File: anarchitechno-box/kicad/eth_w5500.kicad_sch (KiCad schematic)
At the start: 35 parts, among them U16 W5500, U17 ARJM11B1-009-AB-EW2, Y1 25MHz

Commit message: Stijn in de Trein
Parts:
- D8, D9: footprint LED_SMD:LED_0805_2012Metric -> LED_SMD:LED_0603_1608Metric
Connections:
- net +3.3V: no longer C54.1, FB1.1
- net +3V3: now also C54.1, FB1.1
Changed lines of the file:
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@@
 			)
 		)
-		(property "Footprint" "LED_SMD:LED_0805_2012Metric"
+		(property "Footprint" "LED_SMD:LED_0603_1608Metric"
 			(at 152.4 107.95 0)
 			(effects
@@
 	)
 	(symbol
+		(lib_id "power:+3V3")
+		(at 88.9 24.13 0)
+		(unit 1)
+		(exclude_from_sim no)
+		(in_bom yes)
+		(on_board yes)
+		(dnp no)
+		(fields_autoplaced yes)
+		(property "Reference" "#PWR0155"
+			(at 88.9 27.94 0)
+			(effects
+				(font
+					(size 1.27 1.27)
+				)
+				(hide yes)
+			)
+		)
+		(property "Value" "+3V3"
+			(at 88.9 19.05 0)
+			(effects
+				(font
+					(size 1.27 1.27)
+				)
+			)
+		)
+		(property "Footprint" ""
+			(at 88.9 24.13 0)
+			(effects
+				(font
+					(size 1.27 1.27)
+				)
+				(hide yes)
+			)
+		)
+		(property "Datasheet" ""
+			(at 88.9 24.13 0)
+			(effects
+				(font
+					(size 1.27 1.27)
+				)
+				(hide yes)
+			)
+		)
+		(property "Description" "Power symbol creates a global label with name \"+3V3\""
+			(at 88.9 24.13 0)
+			(effects
+				(font
+					(size 1.27 1.27)
+				)
+				(hide yes)
+			)
+		)
+		(pin "1"
+		)
+		(instances
+			(project "anarchytechnobox"
+				(path "/8c734c41-38ed-40fc-83bd-134786dcfb35/fe979741-96bb-4de4-ad6e-25369264489a"
+					(reference "#PWR0155")
+					(unit 1)
+				)
+			)
+		)
+	)
+	(symbol
 		(lib_id "power:GND")
 		(at 46.99 116.84 0)
@@
 			)
 		)
-		(property "Footprint" "LED_SMD:LED_0805_2012Metric"
+		(property "Footprint" "LED_SMD:LED_0603_1608Metric"
 			(at 152.4 113.03 0)
 			(effects
@@
 					(unit 1)
 				)
-			)
-		)
-	)
-	(symbol
-		(lib_id "power:+3.3V")
-		(at 88.9 24.13 0)
-		(unit 1)
-		(exclude_from_sim no)
-		(in_bom yes)
-		(on_board yes)
-		(dnp no)
-		(fields_autoplaced yes)
-		(property "Reference" "#PWR0117"
-			(at 88.9 27.94 0)
-			(effects
-				(font
-					(size 1.27 1.27)
-				)
-				(hide yes)
-			)
-		)
-		(property "Value" "+3.3V"
-			(at 88.9 19.05 0)
-			(effects
-				(font
-					(size 1.27 1.27)
-				)
-			)
-		)
-		(property "Footprint" ""
-			(at 88.9 24.13 0)
-			(effects
-				(font
-					(size 1.27 1.27)
-				)
-				(hide yes)
-			)
-		)
-		(property "Datasheet" ""
-			(at 88.9 24.13 0)
-			(effects
-				(font
-					(size 1.27 1.27)
-				)
-				(hide yes)
-			)
-		)
-		(property "Description" "Power symbol creates a global label with name \"+3.3V\""
-			(at 88.9 24.13 0)
-			(effects
-				(font
-					(size 1.27 1.27)
-				)
-				(hide yes)
-			)
-		)
-		(pin "1"
-		)
-		(instances
-			(project "anarchytechnobox"
-				(path "/8c734c41-38ed-40fc-83bd-134786dcfb35/fe979741-96bb-4de4-ad6e-25369264489a"
-					(reference "#PWR0117")
-					(unit 1)
-				)

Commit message: meer Stijn in de Trein
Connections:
- net +3.3V is gone; now on net +3V3: R30.1, R31.1, R32.1, R33.1, R34.1
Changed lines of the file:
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@@
+	)
+	(symbol
+		(lib_id "power:+3V3")
+		(at 199.39 57.15 0)
+		(unit 1)
+		(exclude_from_sim no)
+		(in_bom yes)
+		(on_board yes)
+		(dnp no)
+		(fields_autoplaced yes)
+		(property "Reference" "#PWR0117"
+			(at 199.39 60.96 0)
+			(effects
+				(font
+					(size 1.27 1.27)
+				)
+				(hide yes)
+			)
+		)
+		(property "Value" "+3V3"
+			(at 199.39 52.07 0)
+			(effects
+				(font
+					(size 1.27 1.27)
+				)
+			)
+		)
+		(property "Footprint" ""
+			(at 199.39 57.15 0)
+			(effects
+				(font
+					(size 1.27 1.27)
+				)
+				(hide yes)
+			)
+		)
+		(property "Datasheet" ""
+			(at 199.39 57.15 0)
+			(effects
+				(font
+					(size 1.27 1.27)
+				)
+				(hide yes)
+			)
+		)
+		(property "Description" "Power symbol creates a global label with name \"+3V3\""
+			(at 199.39 57.15 0)
+			(effects
+				(font
+					(size 1.27 1.27)
+				)
+				(hide yes)
+			)
+		)
+		(pin "1"
+		)
+		(instances
+			(project "anarchytechnobox"
+				(path "/8c734c41-38ed-40fc-83bd-134786dcfb35/fe979741-96bb-4de4-ad6e-25369264489a"
+					(reference "#PWR0117")
+					(unit 1)
+				)
+			)
+		)
 	)
 	(symbol
@@
 					(unit 1)
 				)
-			)
-		)
-	)
-	(symbol
-		(lib_id "power:+3.3V")
-		(at 199.39 57.15 0)
-		(unit 1)
-		(exclude_from_sim no)
-		(in_bom yes)
-		(on_board yes)
-		(dnp no)
-		(fields_autoplaced yes)
-		(property "Reference" "#PWR0129"
-			(at 199.39 60.96 0)
-			(effects
-				(font
-					(size 1.27 1.27)
-				)
-				(hide yes)
-			)
-		)
-		(property "Value" "+3.3V"
-			(at 199.39 52.07 0)
-			(effects
-				(font
-					(size 1.27 1.27)
-				)
-			)
-		)
-		(property "Footprint" ""
-			(at 199.39 57.15 0)
-			(effects
-				(font
-					(size 1.27 1.27)
-				)
-				(hide yes)
-			)
-		)
-		(property "Datasheet" ""
-			(at 199.39 57.15 0)
-			(effects
-				(font
-					(size 1.27 1.27)
-				)
-				(hide yes)
-			)
-		)
-		(property "Description" "Power symbol creates a global label with name \"+3.3V\""
-			(at 199.39 57.15 0)
-			(effects
-				(font
-					(size 1.27 1.27)
-				)
-				(hide yes)
-			)
-		)
-		(pin "1"
-		)
-		(instances
-			(project "anarchytechnobox"
-				(path "/8c734c41-38ed-40fc-83bd-134786dcfb35/fe979741-96bb-4de4-ad6e-25369264489a"
-					(reference "#PWR0129")
-					(unit 1)
-				)

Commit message: trein trein trein
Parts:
- removed C54: 100nF, Capacitor_SMD:C_0402_1005Metric, symbol Device:C
- removed FB1: BLM18PG121SN1D, Inductor_SMD:L_0603_1608Metric, symbol Device:FerriteBead
- added C54, C95: 100n, Capacitor_SMD:C_0402_1005Metric, symbol Device:C_Small
- added C94, C96: 10uF, Capacitor_SMD:C_0603_1608Metric, symbol Device:C
- added L2: BLM18PG121SN1D_C14709, BigFishImports:L0603, symbol BigFishImports:BLM18PG121SN1D_C14709
- added U1: LP5907MFX-3.3, Package_TO_SOT_SMD:SOT-23-5, symbol Regulator_Linear:LP5907MFX-3.3
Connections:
- net +3.3VA: now also C95.2, C96.1, U1.5 (OUT)
- net +3V3: now also U1.3 (EN)
- net GND: now also C54.1, C94.2, C95.1, C96.2, U1.2 (GND)
- new net +5V: L2.1
- new net 5V_ethernet_filtered: C54.2, C94.1, L2.2, U1.1 (IN)

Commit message: 100mbit ethernet jack
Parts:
- U17: footprint Footprints:ARJM11B1-009-AB-EW2 -> parts:ARJM11B1-009-AB-EW2
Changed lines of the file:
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@@
 			)
 		)
-		(property "Footprint" "Footprints:ARJM11B1-009-AB-EW2"
+		(property "Footprint" "parts:ARJM11B1-009-AB-EW2"
 			(at 212.09 74.93 0)
 			(effects

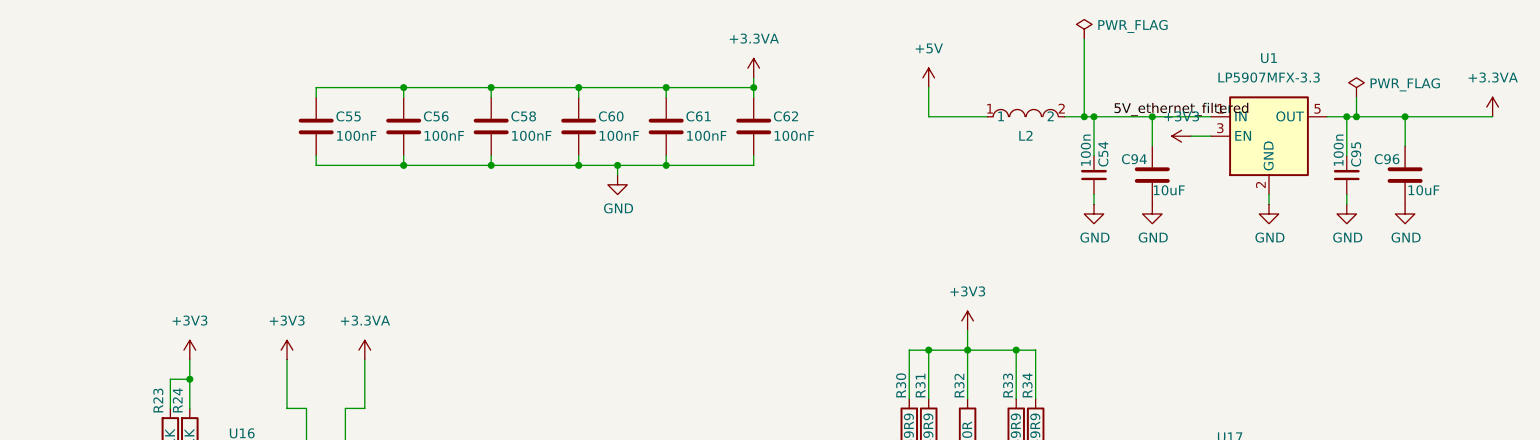
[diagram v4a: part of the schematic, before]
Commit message: Re-added 1.1V regulator. Removed 3.3VDDA for Ethernet. Increased clearances on layout a bit..
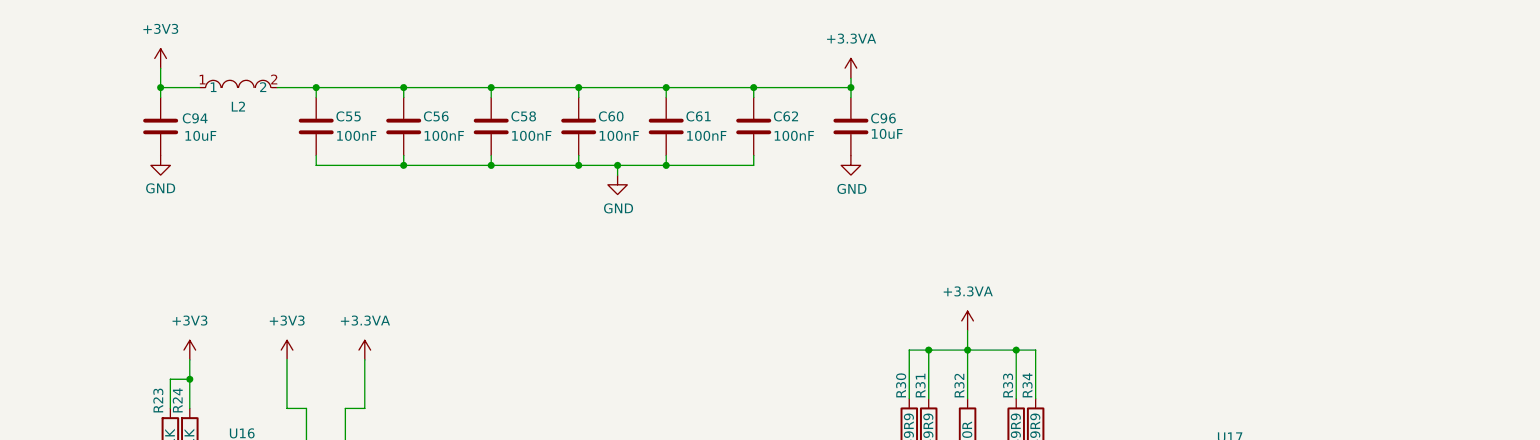
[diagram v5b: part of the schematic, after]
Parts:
- removed C54, C95: 100n, Capacitor_SMD:C_0402_1005Metric, symbol Device:C_Small
- removed U1: LP5907MFX-3.3, Package_TO_SOT_SMD:SOT-23-5, symbol Regulator_Linear:LP5907MFX-3.3
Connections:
- net +5V is gone; now on net +3V3: L2.1
- net +3.3VA: now also L2.2, R30.1, R31.1, R32.1, R33.1, R34.1
- net +3V3: now also C94.1; no longer R30.1, R31.1, R32.1, R33.1, R34.1
- removed net 5V_ethernet_filtered: C94.1, L2.2
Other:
- moved on the sheet: C94, C96, L2

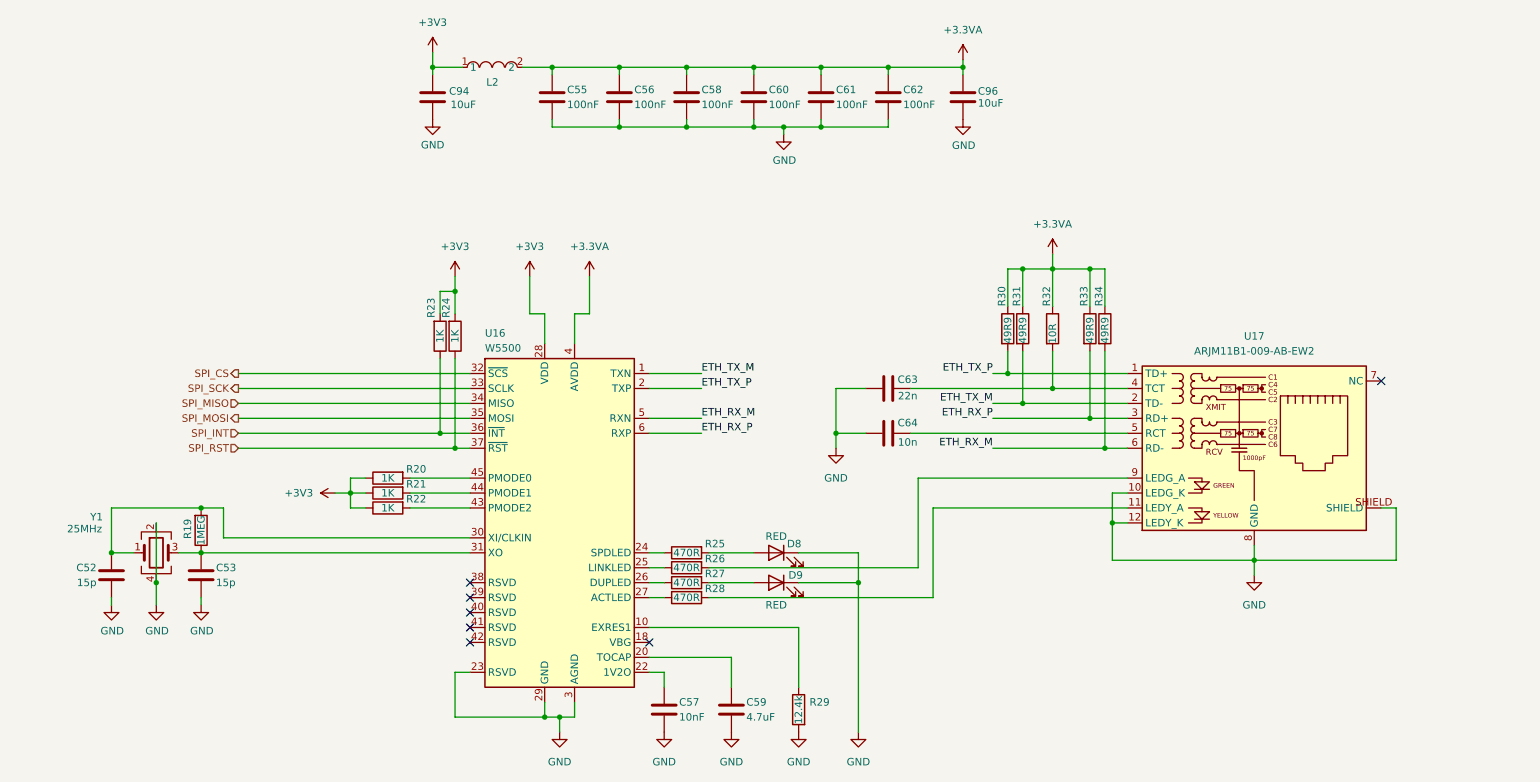
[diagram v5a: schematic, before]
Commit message: Schematic & PCB changes: - Cleaned up unnecessary electrolytic input capacitor flyback - Removed dual diode rectification on 5V, increased output capacitors - Feedback resistors DC/DCs set, enlarged for JLC basic parts - Sweep through schematic to consolidate caps to JLC basic parts (see list schematic front page) - Midi OUTPUT added (please check schematic) - Wiznet W5500 schematic reworked to RJ45 reference schematic: https://docs.wiznet.io/assets/files/w5500_sch_v110_use_mag_-dfff8bbb103d13be4f25cd2b2f8b950d.pdf - Replaced ethernet jack to HR911105A - Crystals chosen for W5500 and RP2350B (according to reference), 15pF load caps. - RS485 driver changed to SP3485EN for 3.3V operation - Replaced RS485 bus connectors with 2x RJ45s for passthrough - Groove connector replaced with JST XH 2mm - Added LCSC part numbers for various components in the schematic
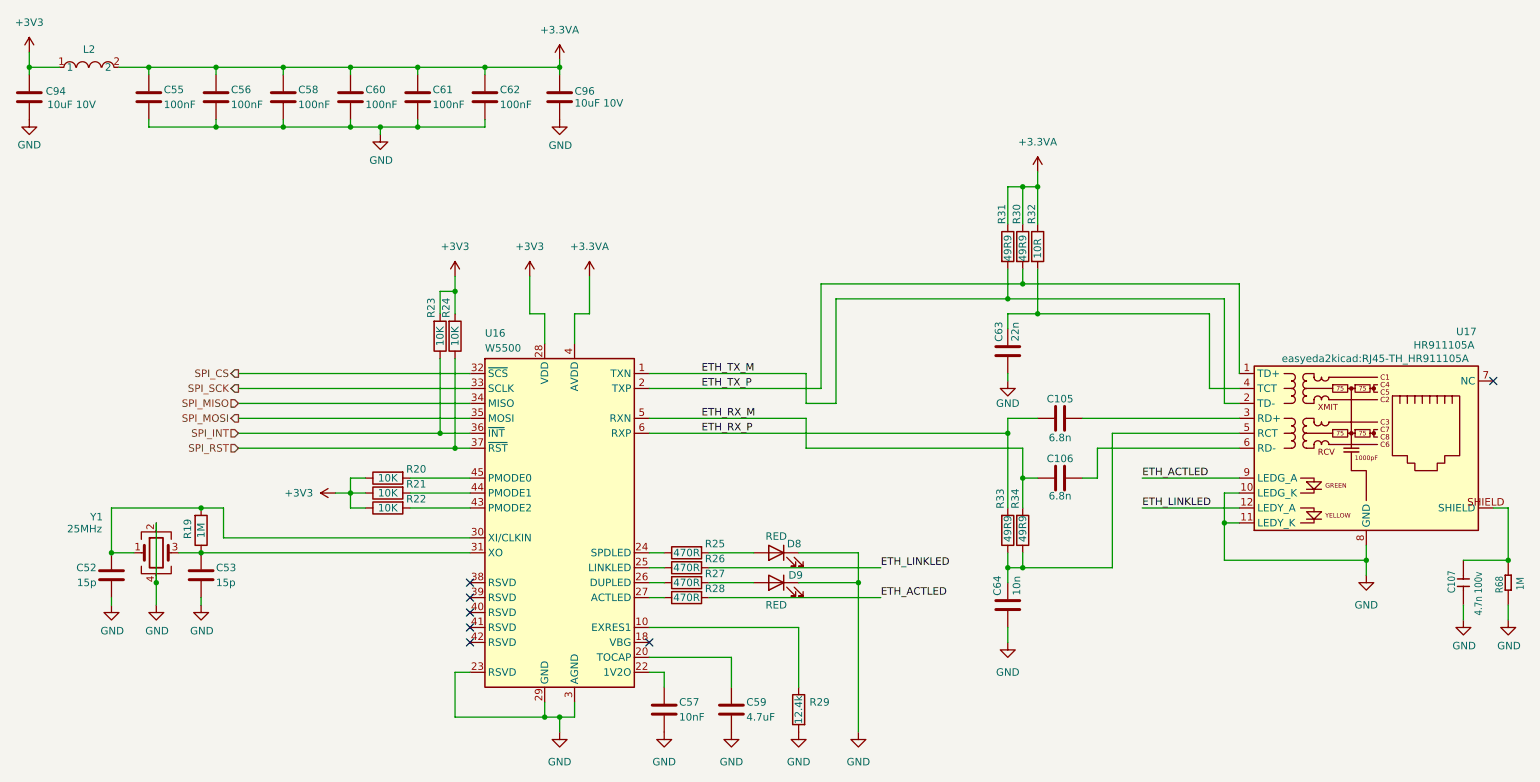
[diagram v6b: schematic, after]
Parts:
- added C105, C106: 6.8n, Capacitor_SMD:C_0603_1608Metric, symbol Device:C
- added C107: 4.7n 100v, Capacitor_SMD:C_1206_3216Metric, symbol TINRS - Wobbler (pico)sch-eagle-import:C-1206
- added R68: 1M, Resistor_SMD:R_0603_1608Metric, symbol TINRS - Wobbler (pico)sch-eagle-import:R-0603
- C52, C53: LCSC Part (none) -> C1548
- C57, C64: LCSC Part (none) -> C15195
- C59: LCSC Part (none) -> C19666
- C63: LCSC Part (none) -> C1532
- C94, C96: value 10uF -> 10uF 10V; Digi-Key_PN 311-1344-1-ND -> (none); LCSC Part (none) -> C19702
- L2: footprint BigFishImports:L0603 -> Inductor_SMD:L_0603_1608Metric
- R19: value 1MEG -> 1M; LCSC Part (none) -> C26083
- R20, R21, R22, R23, R24: value 1K -> 10K
- R29: LCSC Part (none) -> C11692
- R30, R31, R33, R34: LCSC Part (none) -> C25120
- R32: LCSC Part (none) -> C25077
- U17: value ARJM11B1-009-AB-EW2 -> HR911105A; footprint parts:ARJM11B1-009-AB-EW2 -> easyeda2kicad:RJ45-TH_HR911105A; LCSC Part (none) -> C12074
- Y1: LCSC Part (none) -> C9006
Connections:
- net +3.3VA: no longer R33.1, R34.1
- net ETH_RX_M: now also C106.1; no longer U17.6 (RD-)
- net ETH_RX_P: now also C105.1; no longer U17.3 (RD+)
- net GND: now also U17.11 (LEDY_K), C107.1, R68.1; no longer U17.12 (LEDY_K), U17.SHIELD
- net ETH_ACTLED: now reaches U17.9 (LEDG_A)
- net ETH_ACTLED: now also R28.2; no longer R26.2
- net at C64.2, U17.5 (RCT): now also R33.1, R34.1
- new net: C106.2, U17.6 (RD-)
- new net: C107.2, R68.2, U17.SHIELD
- new net: C105.2, U17.3 (RD+)
- new net ETH_LINKLED: R26.2, U17.12 (LEDY_A)
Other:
- moved on the sheet: C55, C56, C58, C60, C61, C62, C63, C64, C94, C96, L2, R30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

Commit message: BOM nagelopen, bestelklaar.
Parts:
- U16: LCSC Part (none) -> C32843
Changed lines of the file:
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@@
+			)
+		)
+		(property "LCSC Part" "C32843"
+			(at 115.57 102.87 0)
+			(effects
+				(font
+					(size 1.27 1.27)
+				)
+				(hide yes)
 			)
 		)

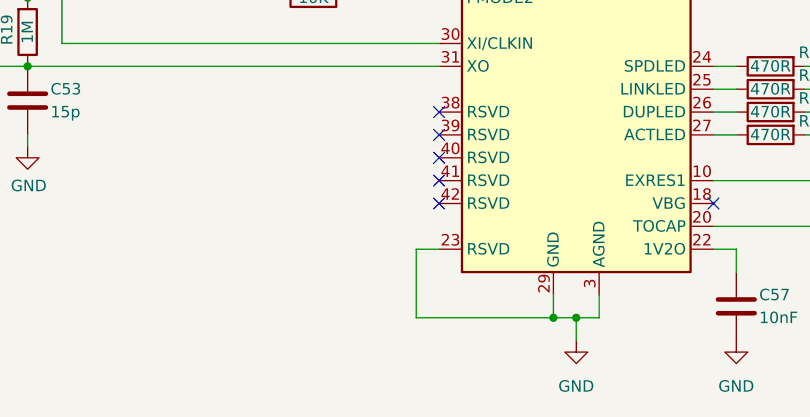
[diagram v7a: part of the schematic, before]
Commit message: 10k W5500 on RSVD pin
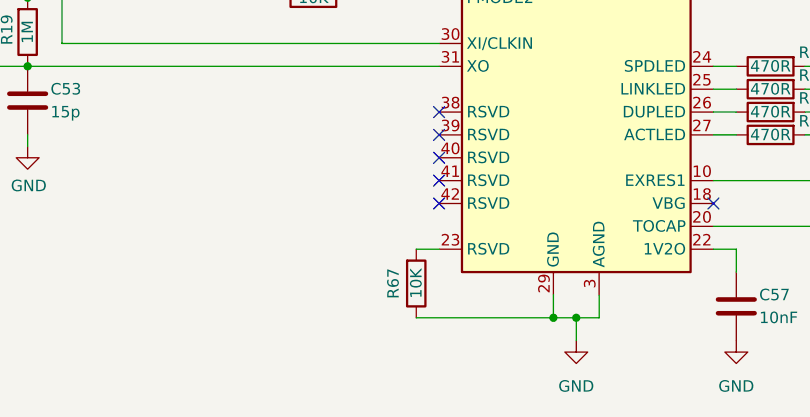
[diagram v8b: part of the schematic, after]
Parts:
- added R67: 10K, Resistor_SMD:R_0402_1005Metric, symbol Device:R
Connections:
- net GND: now also R67.1; no longer U16.23 (RSVD)
- new net: R67.2, U16.23 (RSVD)
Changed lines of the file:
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@@
 	(wire
 		(pts
-			(xy 97.79 128.27) (xy 97.79 135.89)
-		)
-		(stroke
-			(width 0)
-			(type default)
-		)
-	)
-	(wire
-		(pts
 			(xy 166.37 113.03) (xy 156.21 113.03)
 		)
@@
 					(unit 1)
 				)
+			)
+		)
+	)
+	(symbol
+		(lib_id "Device:R")
+		(at 97.79 132.08 0)
+		(mirror x)
+		(unit 1)
+		(exclude_from_sim no)
+		(in_bom yes)
+		(on_board yes)
+		(dnp no)
+		(property "Reference" "R67"
+			(at 95.25 132.08 90)
+			(effects
+				(font
+					(size 1.27 1.27)
+				)
+			)
+		)
+		(property "Value" "10K"
+			(at 97.79 132.08 90)
+			(effects
+				(font
+					(size 1.27 1.27)
+				)
+			)
+		)
+		(property "Footprint" "Resistor_SMD:R_0402_1005Metric"
+			(at 96.012 132.08 90)
+			(effects
+				(font
+					(size 1.27 1.27)
+				)
+				(hide yes)
+			)
+		)
+		(property "Datasheet" "~"
+			(at 97.79 132.08 0)
+			(effects
+				(font
+					(size 1.27 1.27)
+				)
+				(hide yes)
+			)
+		)
+		(property "Description" "Resistor"
+			(at 97.79 132.08 0)
+			(effects
+				(font
+					(size 1.27 1.27)
+				)
+				(hide yes)
+			)
+		)
+		(pin "1"
+		)
+		(pin "2"
+		)
+		(instances
+			(project "anarchytechnobox"
+				(path "/8c734c41-38ed-40fc-83bd-134786dcfb35/fe979741-96bb-4de4-ad6e-25369264489a"
+					(reference "R67")
+					(unit 1)
+				)
